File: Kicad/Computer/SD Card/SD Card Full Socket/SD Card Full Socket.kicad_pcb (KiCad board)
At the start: 2 copper layers, 36.6 x 58.4 mm, 15 parts, among them IC1 AP7365-33WG-7, IC2 CBT3244AD,112, J1 SDK-9BNS-K13-GS-TB_LF__SN_1, J5 Conn_01x20, J6 Conn_01x20

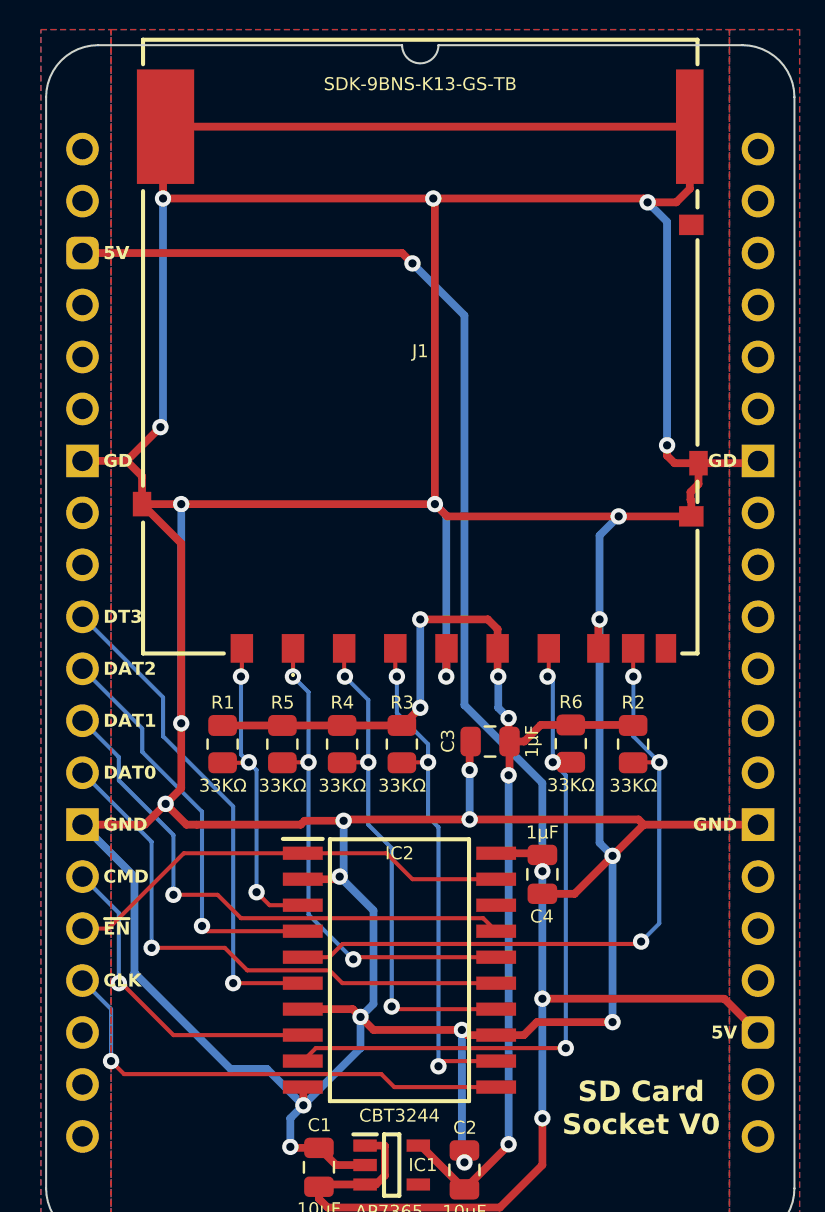
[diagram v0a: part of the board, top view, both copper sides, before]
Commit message: Generated Gerbers for SD Card components.
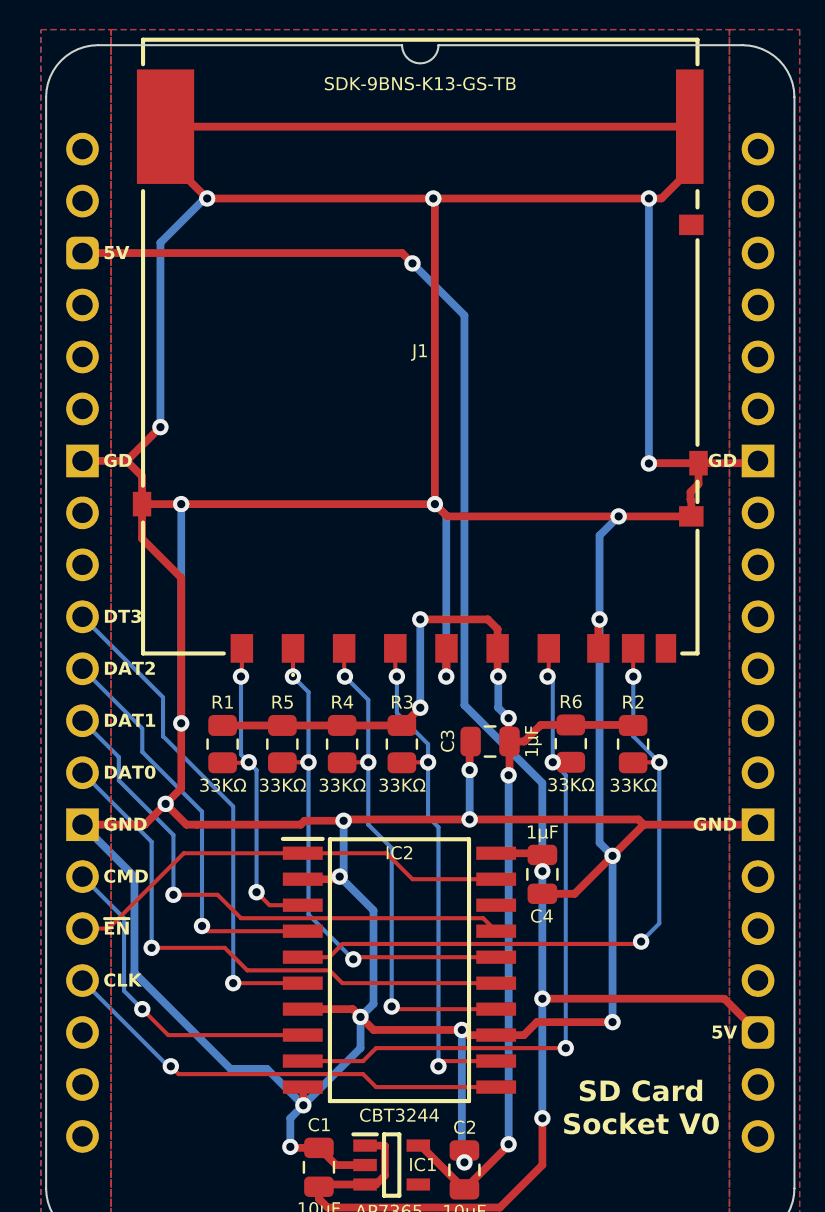
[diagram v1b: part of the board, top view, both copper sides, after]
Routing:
- net GND: track 313.3 -> 309.9 mm
- net SD CLK: track 23.9 -> 22.4 mm
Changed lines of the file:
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@@
 	)
 	(segment
-		(start 116.332 94.234)
-		(end 116.205 94.107)
+		(start 118.491 96.647)
+		(end 117.221 95.377)
 		(width 0.2)
 		(layer "F.Cu")
@@
 	)
 	(segment
-		(start 116.205 94.107)
-		(end 116.078 94.107)
+		(start 125.699 96.647)
+		(end 118.491 96.647)
 		(width 0.2)
 		(layer "F.Cu")
 		(net 5)
 	)
-	(segment
-		(start 125.699 96.647)
-		(end 118.745 96.647)
-		(width 0.2)
-		(layer "F.Cu")
+	(via
+		(at 117.221 95.377)
+		(size 0.8)
+		(drill 0.4)
+		(layers "F.Cu" "B.Cu")
 		(net 5)
 	)
 	(segment
-		(start 118.745 96.647)
-		(end 116.332 94.234)
-		(width 0.2)
-		(layer "F.Cu")
+		(start 114.3 88.9)
+		(end 116.332 90.932)
+		(width 0.2)
+		(layer "B.Cu")
 		(net 5)
 	)
-	(via
-		(at 116.078 94.107)
-		(size 0.8)
-		(drill 0.4)
-		(layers "F.Cu" "B.Cu")
+	(segment
+		(start 116.332 90.932)
+		(end 116.332 94.488)
+		(width 0.2)
+		(layer "B.Cu")
 		(net 5)
 	)
 	(segment
-		(start 114.3 88.9)
-		(end 116.078 90.678)
-		(width 0.2)
-		(layer "B.Cu")
-		(net 5)
-	)
-	(segment
-		(start 116.078 90.678)
-		(end 116.078 94.107)
+		(start 116.332 94.488)
+		(end 117.221 95.377)
 		(width 0.2)
 		(layer "B.Cu")
@@
 	)
 	(segment
+		(start 119.126 81.407)
+		(end 119.126 74.295)
+		(width 0.38)
+		(layer "F.Cu")
+		(net 11)
+	)
+	(segment
 		(start 144.41 68.692)
 		(end 144.41 69.712)
@@
 	)
 	(segment
-		(start 143.241 68.692)
-		(end 142.875 68.326)
-		(width 0.38)
-		(layer "F.Cu")
-		(net 11)
-	)
-	(segment
 		(start 140.507 71.292)
 		(end 144.06 71.292)
@@
 	)
 	(segment
-		(start 131.445 55.753)
-		(end 141.732 55.753)
+		(start 118.237 53.594)
+		(end 120.396 55.753)
 		(width 0.38)
 		(layer "F.Cu")
@@
 	)
 	(segment
-		(start 141.732 55.753)
-		(end 141.9225 55.9435)
+		(start 119.126 74.295)
+		(end 117.21 72.379)
 		(width 0.38)
 		(layer "F.Cu")
@@
 	)
 	(segment
-		(start 144.41 68.692)
-		(end 143.241 68.692)
-		(width 0.38)
-		(layer "F.Cu")
-		(net 11)
-	)
-	(segment
-		(start 118.237 55.753)
-		(end 131.445 55.753)
-		(width 0.38)
-		(layer "F.Cu")
-		(net 11)
-	)
-	(segment
-		(start 143.3195 55.9435)
-		(end 141.9225 55.9435)
-		(width 0.38)
-		(layer "F.Cu")
-		(net 11)
-	)
-	(segment
 		(start 134.519 96.647)
 		(end 133.096 96.647)
@@
 	)
 	(segment
-		(start 119.126 72.608)
-		(end 117.21 70.692)
-		(width 0.38)
-		(layer "F.Cu")
-		(net 11)
-	)
-	(segment
 		(start 132.842 96.393)
 		(end 128.524 96.393)
@@
 	)
 	(segment
+		(start 142.599 55.753)
+		(end 141.986 55.753)
+		(width 0.38)
+		(layer "F.Cu")
+		(net 11)
+	)
+	(segment
 		(start 136.779 89.739)
 		(end 138.353 89.739)
@@
 	)
 	(segment
-		(start 142.875 68.326)
-		(end 142.875 67.818)
-		(width 0.38)
-		(layer "F.Cu")
-		(net 11)
-	)
-	(segment
 		(start 144.41 68.692)
 		(end 147.208 68.692)
@@
 	)
 	(segment
-		(start 119.126 81.407)
-		(end 119.126 72.608)
-		(width 0.38)
-		(layer "F.Cu")
-		(net 11)
-	)
-	(segment
 		(start 141.732 86.36)
 		(end 147.32 86.36)
@@
 	)
 	(segment
+		(start 131.445 55.753)
+		(end 120.396 55.753)
+		(width 0.38)
+		(layer "F.Cu")
+		(net 11)
+	)
+	(segment
 		(start 136.509008 96.011992)
 		(end 140.208 96.011992)
@@
 	)
 	(segment
-		(start 118.237 55.753)
-		(end 118.237 52.365001)
+		(start 131.445 55.753)
+		(end 141.986 55.753)
 		(width 0.38)
 		(layer "F.Cu")
@@
 	)
 	(segment
+		(start 143.985 54.367)
+		(end 142.599 55.753)
+		(width 0.38)
+		(layer "F.Cu")
+		(net 11)
+	)
+	(segment
 		(start 132.125 71.292)
 		(end 131.524999 70.691999)
@@
 	)
 	(segment
-		(start 143.985 55.278)
-		(end 143.3195 55.9435)
+		(start 144.41 68.692)
+		(end 142.000996 68.692)
 		(width 0.38)
 		(layer "F.Cu")
@@
 	)
 	(segment
-		(start 143.985 52.242)
-		(end 143.985 55.278)
+		(start 117.21 72.379)
+		(end 117.21 70.692)
 		(width 0.38)
 		(layer "F.Cu")
@@
 	)
 	(segment
+		(start 142.000996 68.692)
+		(end 141.985996 68.707)
+		(width 0.38)
+		(layer "F.Cu")
+		(net 11)
+	)
+	(segment
 		(start 134.519 96.647)
 		(end 135.874 96.647)
@@
 	)
 	(via
-		(at 142.875 67.818)
+		(at 141.985996 68.707)
 		(size 0.8)
 		(drill 0.4)
@@
 	)
 	(via
-		(at 118.237 55.753)
+		(at 120.396 55.753)
 		(size 0.8)
 		(drill 0.4)
@@
 	)
 	(via
-		(at 141.9225 55.9435)
+		(at 141.986 55.753)
 		(size 0.8)
 		(drill 0.4)
@@
 	)
 	(segment
-		(start 118.237 66.802)
-		(end 118.109997 66.929003)
-		(width 0.38)
-		(layer "B.Cu")
-		(net 11)
-	)
-	(segment
 		(start 133.223 86.106)
 		(end 133.223 83.693)
@@
 	)
 	(segment
+		(start 141.985996 55.753004)
+		(end 141.986 55.753)
+		(width 0.38)
+		(layer "B.Cu")
+		(net 11)
+	)
+	(segment
 		(start 114.3 86.36)
 		(end 116.84 88.9)
@@
 	)
 	(segment
+		(start 141.985996 68.707)
+		(end 141.985996 55.753004)
+		(width 0.38)
+		(layer "B.Cu")
+		(net 11)
+	)
+	(segment
+		(start 118.109997 66.929003)
+		(end 118.109997 57.912003)
+		(width 0.38)
+		(layer "B.Cu")
+		(net 11)
+	)
+	(segment
 		(start 124.46 102.108)
 		(end 124.46 100.711)
@@
 	)
 	(segment
-		(start 142.875 56.896)
-		(end 141.9225 55.9435)
-		(width 0.38)
-		(layer "B.Cu")
-		(net 11)
-	)
-	(segment
 		(start 139.573 76.327)
 		(end 139.573 72.226)
@@
 	)
 	(segment
+		(start 118.109997 57.912003)
+		(end 120.269 55.753)
+		(width 0.38)
+		(layer "B.Cu")
+		(net 11)
+	)
+	(segment
 		(start 139.573 76.327)
 		(end 139.573 87.249)
@@
 	)
 	(segment
-		(start 118.237 55.753)
-		(end 118.237 66.802)
-		(width 0.38)
-		(layer "B.Cu")
-		(net 11)
-	)
-	(segment
 		(start 132.08 79.121)
 		(end 132.08 71.247)
@@
 	)
 	(segment
-		(start 142.875 67.818)
-		(end 142.875 56.896)
+		(start 120.269 55.753)
+		(end 120.396 55.753)
 		(width 0.38)
 		(layer "B.Cu")
@@
 	)
 	(segment
-		(start 129.54 99.187)
-		(end 128.905 98.552)
+		(start 134.519 99.187)
+		(end 128.651 99.187)
 		(width 0.2)
 		(layer "F.Cu")
@@
 	)
 	(segment
-		(start 116.332 98.552)
-		(end 115.697 97.917)
+		(start 128.016 98.552)
+		(end 118.999 98.552)
 		(width 0.2)
 		(layer "F.Cu")
@@
 	)
 	(segment
-		(start 128.905 98.552)
-		(end 116.332 98.552)
+		(start 128.651 99.187)
+		(end 128.016 98.552)
 		(width 0.2)
 		(layer "F.Cu")
@@
 	)
 	(segment
-		(start 134.519 99.187)
-		(end 129.54 99.187)
+		(start 118.999 98.552)
+		(end 118.618 98.171)
 		(width 0.2)
 		(layer "F.Cu")
@@
 	)
 	(via
-		(at 115.697 97.917)
+		(at 118.618 98.171)
 		(size 0.8)
 		(drill 0.4)
@@
 	)
 	(segment
+		(start 118.491 98.171)
+		(end 118.618 98.171)
+		(width 0.2)
+		(layer "B.Cu")
+		(net 15)
+	)
+	(segment
 		(start 114.3 93.98)
-		(end 115.697 95.377)
-		(width 0.2)
-		(layer "B.Cu")
-		(net 15)
-	)
-	(segment
-		(start 115.697 95.377)
-		(end 115.697 97.917)
+		(end 118.491 98.171)
 		(width 0.2)
 		(layer "B.Cu")
@@
 	)
 	(segment
+		(start 128.016 97.917)
+		(end 128.651 97.282)
+		(width 0.2)
+		(layer "F.Cu")
+		(net 18)
+	)
+	(segment
 		(start 137.287 83.312)
 		(end 138.166 83.312)
@@
 	(segment
 		(start 125.069 97.917)
-		(end 125.704 97.282)
+		(end 128.016 97.917)
 		(width 0.2)
 		(layer "F.Cu")
@@
 	)
 	(segment
-		(start 125.704 97.282)
+		(start 128.651 97.282)
 		(end 137.922 97.282)
 		(width 0.2)

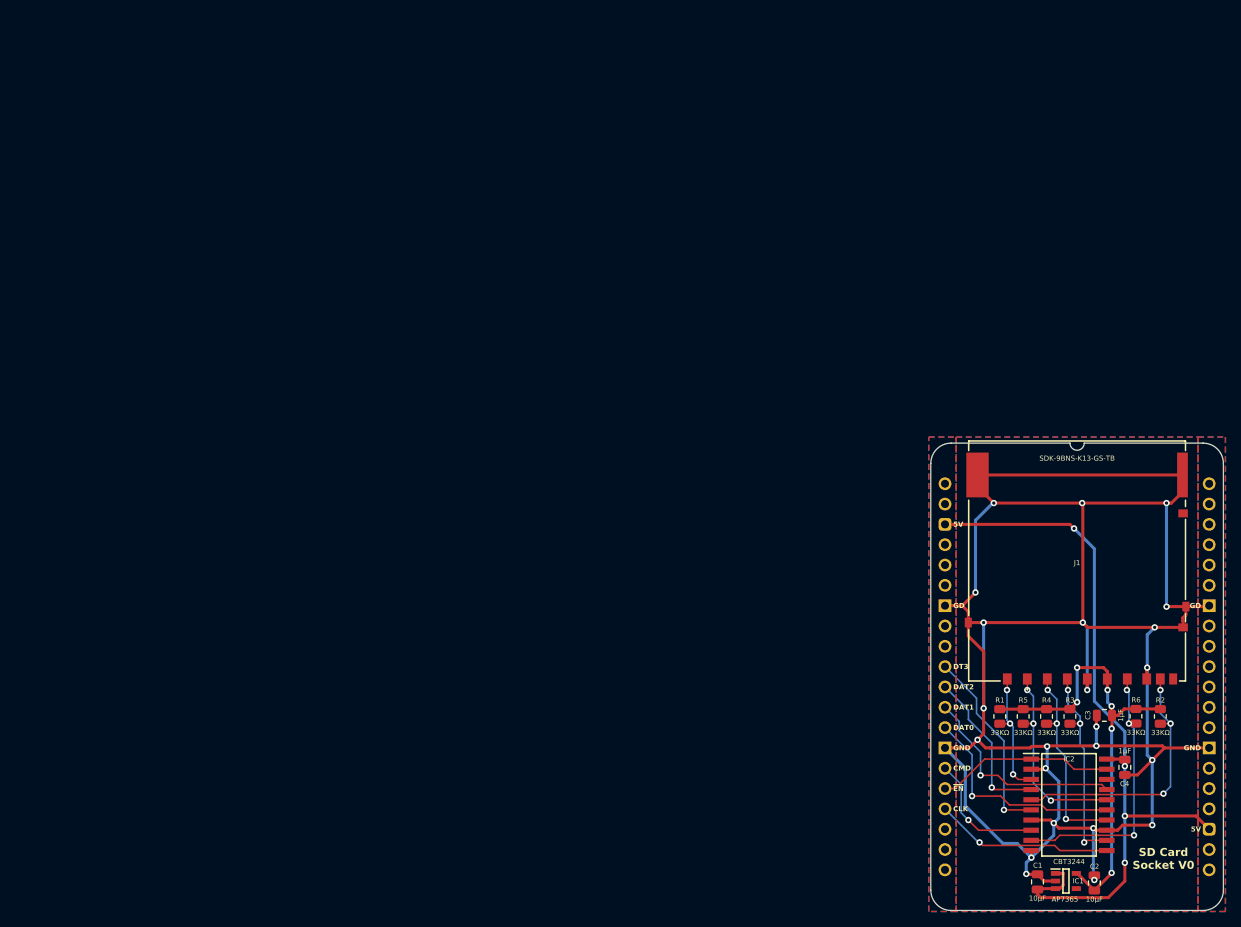
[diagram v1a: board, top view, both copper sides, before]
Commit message: Use VRML instead of STEPs for SD Card Board models.
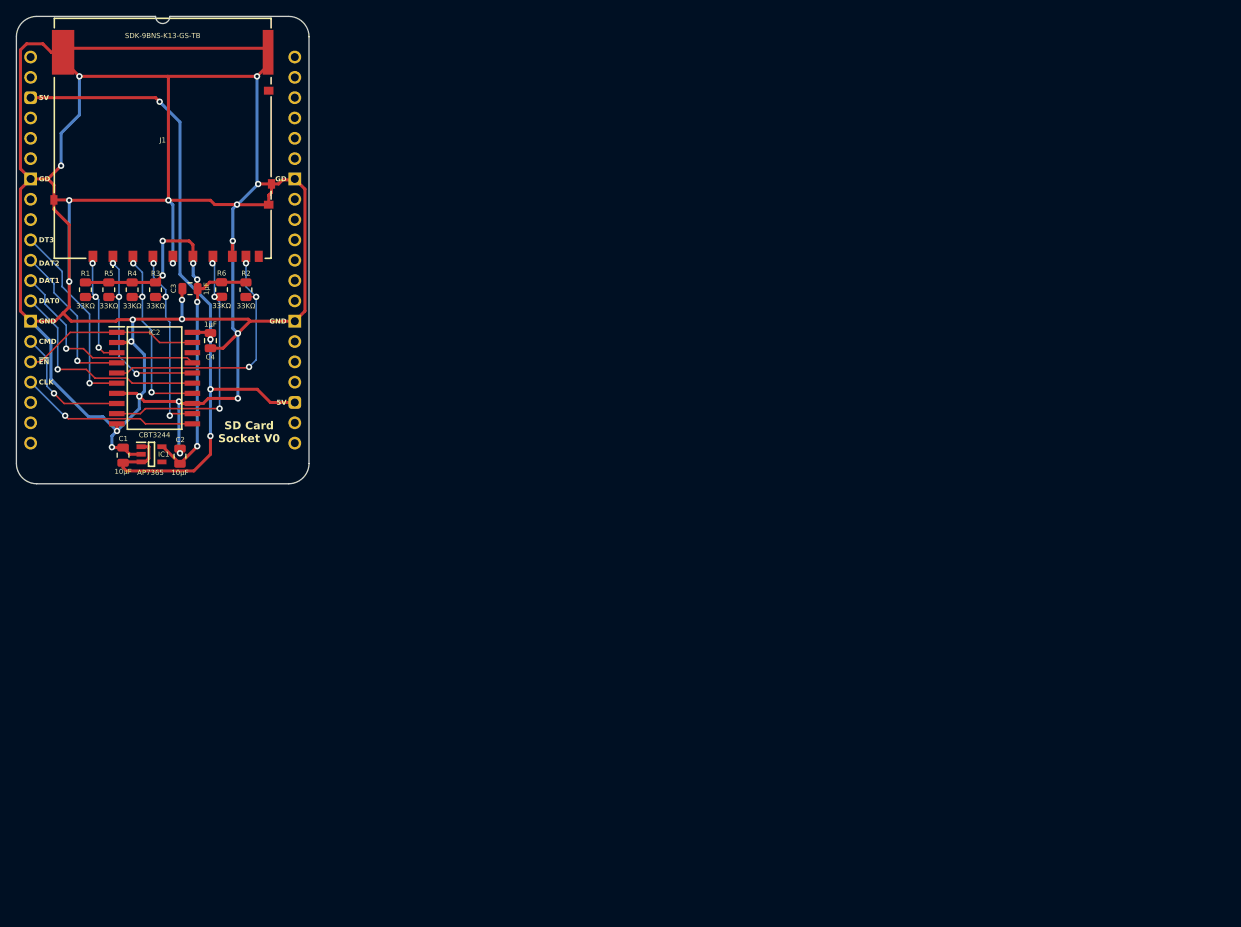
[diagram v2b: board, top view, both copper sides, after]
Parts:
- added J2: Pin_Header_01x20, SamacSys_Parts:PinHeader_1x20_P2.54mm_Vertical, B.Cu at (0.00, 0.00)
- added J3: Pin_Header_01x20, SamacSys_Parts:PinHeader_1x20_P2.54mm_Vertical, B.Cu at (33.0, 0.00)
- moved C3 126.1 mm to (19.9, 29.0)
- moved IC1 126.1 mm to (15.1, 49.7)
- moved C2 126.1 mm to (18.7, 49.9)
- moved J5 126.1 mm to (0.00, 0.00)
- moved R1 126.1 mm to (6.86, 29.1)
- moved R3 126.1 mm to (15.6, 29.1)
- moved R4 126.1 mm to (12.7, 29.1)
- moved R5 126.1 mm to (9.78, 29.1)
- moved IC2 126.1 mm to (15.5, 40.1)
- moved J6 126.1 mm to (33.0, 48.3)
- moved R2 126.1 mm to (26.9, 29.1)
- moved R6 126.1 mm to (23.9, 29.1)
- moved C1 126.1 mm to (11.6, 49.8)
- moved C4 126.1 mm to (22.5, 35.4)
- moved J1 125.9 mm to (16.5, 10.2)
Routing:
- net GND: track 309.9 -> 372.2 mm, vias 23 -> 21
- net Net-(IC2-2B4): track 16.1 -> 15.6 mm
- net Net-(IC2-1B3): track 24.9 -> 24.4 mm
- net Net-(IC2-1B2): track 24.7 -> 24.2 mm
- net Net-(IC2-2B3): track 33.3 -> 32.8 mm
- net Net-(IC2-1B4): track 25.5 -> 25.0 mm
- removed copper zone on B.Cu, net GND
- removed copper zone on F.Cu, net GND

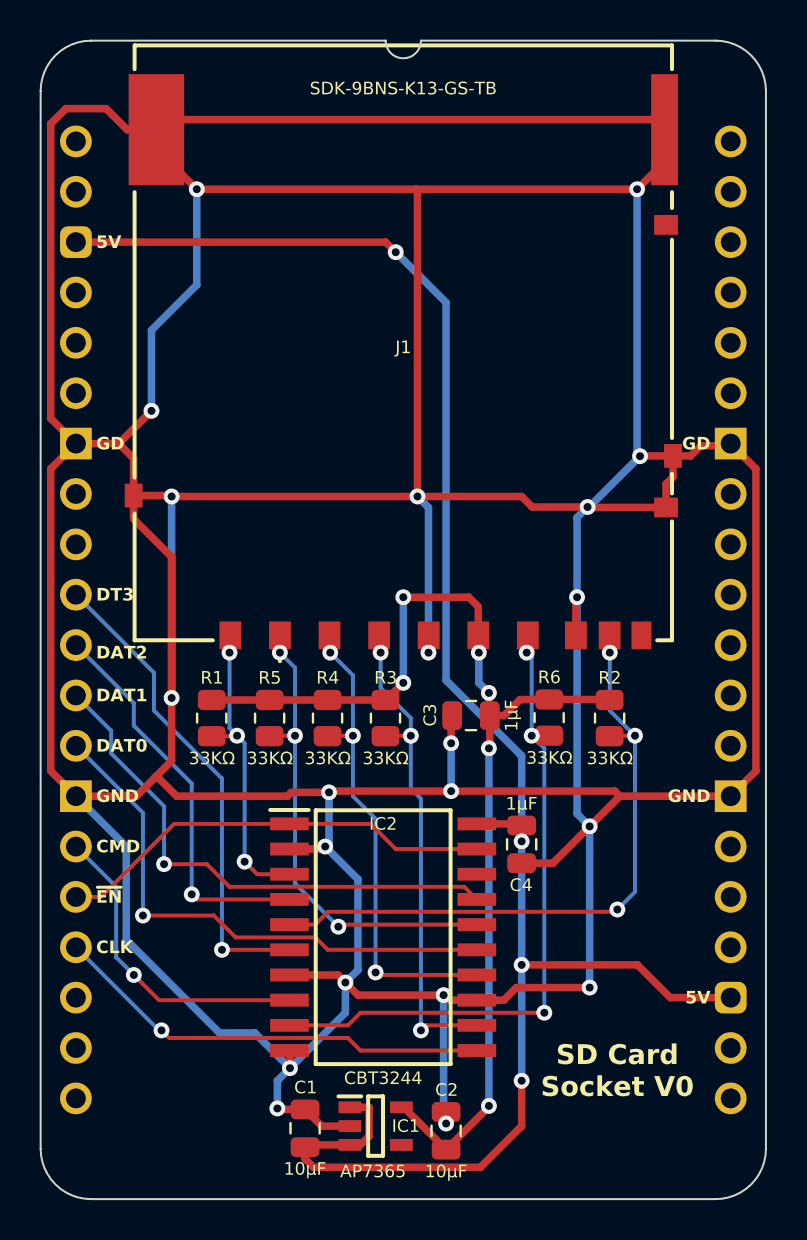
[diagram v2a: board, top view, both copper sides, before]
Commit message: Rounded SD Card Write traces.
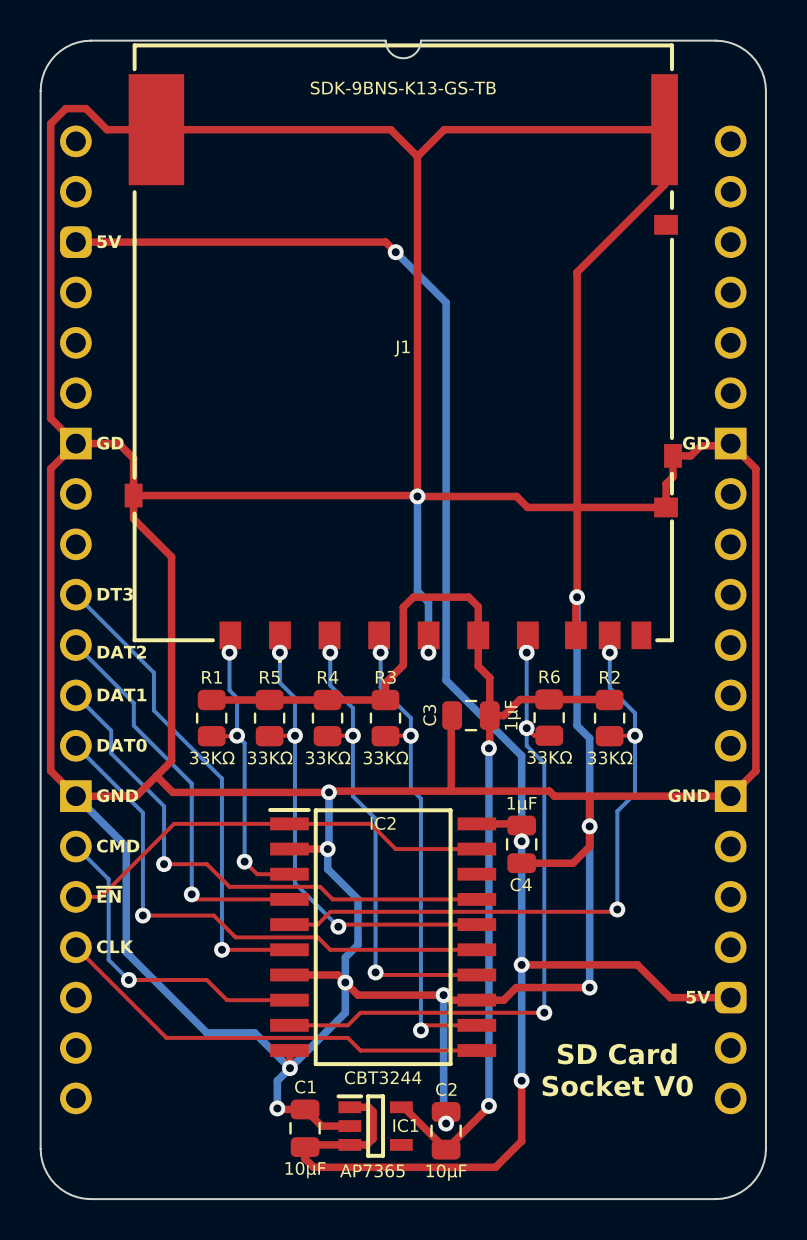
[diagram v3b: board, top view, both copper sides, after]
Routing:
- net GND: track 372.2 -> 325.0 mm, vias 21 -> 12
- net 5V: track 95.5 -> 96.3 mm
- net /3.3V: track 56.1 -> 55.9 mm, vias 6 -> 2
- net SD CLK: vias 1 -> 0
